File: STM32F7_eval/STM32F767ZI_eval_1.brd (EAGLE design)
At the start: 76.2 x 53.3 mm, 101 parts, among them CN3 GROVE-4P-CONN-I2C-90D, CN4 GROVE-4P-CONN-I2C-90D, CN5 ARDUINO_COMPAT_IF, CN6 STLINKV21_SWD_IF, CN7 WFT0750CZ09-SMD_, CN9 UART_IF, Q1 PMF370XN_, SW1 SKRPACE010_, SW2 SKRPACE010_, U1 STM32F767ZI_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

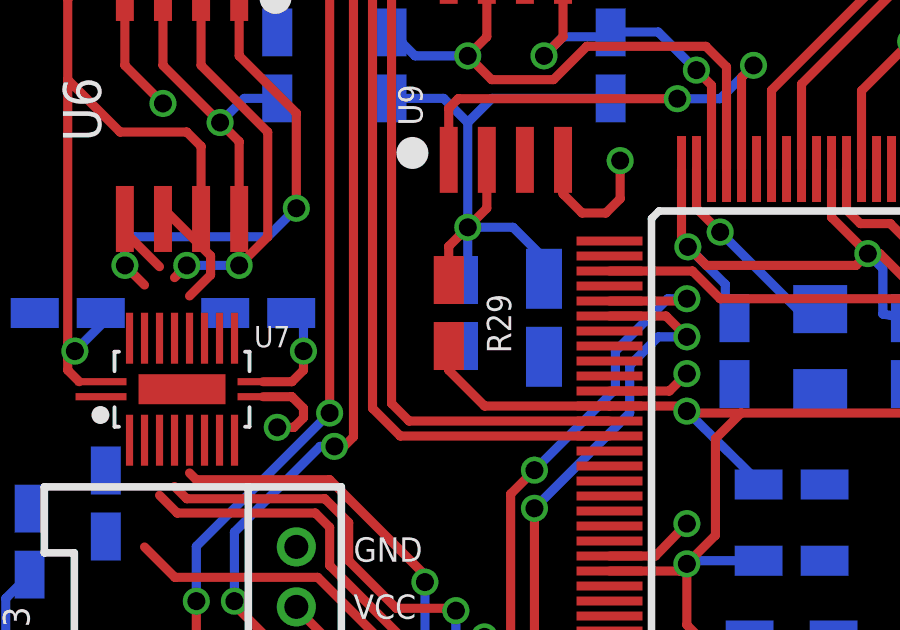
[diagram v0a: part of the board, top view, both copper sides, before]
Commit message: 回路図を修正
・回路図のレイアウトを修正
・定数変更
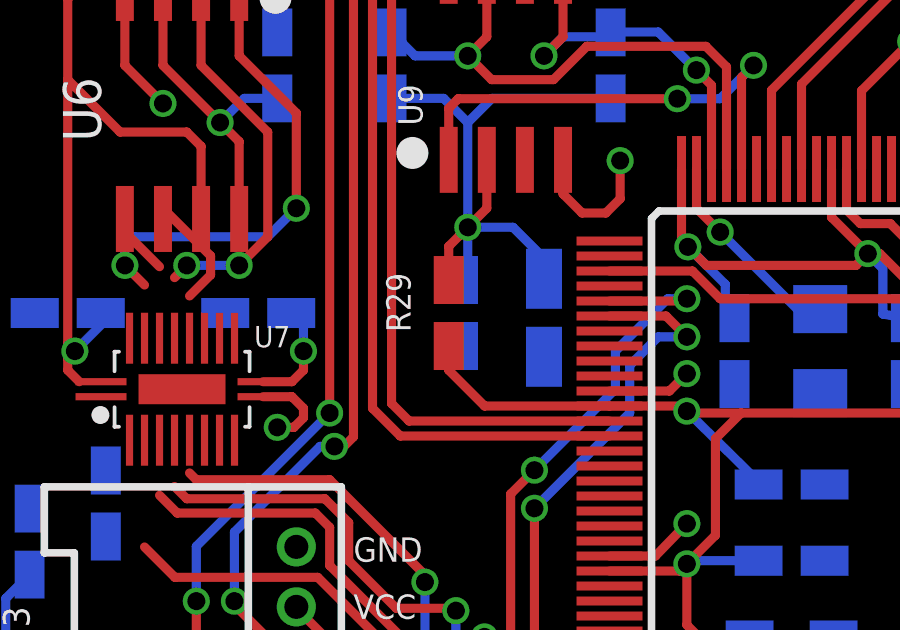
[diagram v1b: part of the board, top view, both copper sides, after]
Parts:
- R27, R28: value 3.3k -> 2.2k
- turned R29 to 90 degrees
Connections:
- net VCC_STSAFE: now also R29.2; no longer R29.1
- net VDD: now also R29.1; no longer R29.2
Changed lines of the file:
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@@
 <element name="C47" library="Parts" package="SMD_1608_DEV" value="0.1uF" x="15.71625" y="35.56" rot="MR270"/>
 <element name="C48" library="Parts" package="SMD_2012_DEV" value="10uF" x="18.415" y="35.40125" rot="MR270"/>
-<element name="R27" library="Parts" package="SMD_1608_DEV" value="3.3k" x="13.335" y="43.815" rot="MR270"/>
-<element name="R28" library="Parts" package="SMD_1608_DEV" value="3.3k" x="20.6375" y="43.815" rot="MR270"/>
+<element name="R27" library="Parts" package="SMD_1608_DEV" value="2.2k" x="13.335" y="43.815" rot="MR270"/>
+<element name="R28" library="Parts" package="SMD_1608_DEV" value="2.2k" x="20.6375" y="43.815" rot="MR270"/>
 <element name="U9" library="Parts" package="SO8N" value="STSAFE" x="17.145" y="43.815"/>
-<element name="R29" library="Parts" package="SMD_1608_DEV" value="0" x="15.24" y="35.56" rot="R270"/>
+<element name="R29" library="Parts" package="SMD_1608_DEV" value="0" x="15.24" y="35.56" rot="R90"/>
 <element name="U5" library="Parts" package="SC-70-5_DEV" value="MIC5366-1.8YC5_" x="-3.96875" y="-9.525"/>
 <element name="C28" library="Parts" package="SMD_1608_DEV" value="1uF X5R" x="-1.905" y="-24.4475"/>
@@
 <contactref element="U5" pad="2"/>
 <contactref element="C46" pad="2"/>
-<wire x1="71.585" y1="44.45" x2="71.585" y2="46.99" width="0" layer="19" extent="1-1"/>
-<wire x1="73.69" y1="35.2425" x2="73.37" y2="35.27" width="0" layer="19" extent="1-16"/>
-<wire x1="73.69" y1="39.0525" x2="74.295" y2="37.465" width="0" layer="19" extent="1-16"/>
-<wire x1="73.69" y1="32.385" x2="74.295" y2="34.6075" width="0" layer="19" extent="1-16"/>
-<wire x1="73.69" y1="24.4475" x2="73.69" y2="21.59" width="0" layer="19" extent="1-16"/>
-<wire x1="73.025" y1="6.6675" x2="73.46" y2="9.93" width="0" layer="19" extent="1-1"/>
-<wire x1="73.69" y1="27.94" x2="73.69" y2="24.4475" width="0" layer="19" extent="16-16"/>
-<wire x1="62.835" y1="28.8925" x2="68.74" y2="30.77" width="0" layer="19" extent="1-16"/>
-<wire x1="62.835" y1="33.02" x2="62.835" y2="28.8925" width="0" layer="19" extent="16-16"/>
-<wire x1="58.885" y1="33.27" x2="62.835" y2="33.02" width="0" layer="19" extent="16-16"/>
-<wire x1="58.885" y1="30.48" x2="58.885" y2="33.27" width="0" layer="19" extent="16-16"/>
-<wire x1="57.965" y1="29.845" x2="58.885" y2="30.48" width="0" layer="19" extent="1-16"/>
-<wire x1="58.885" y1="26.035" x2="57.965" y2="26.67" width="0" layer="19" extent="1-16"/>
-<wire x1="58.885" y1="21.9075" x2="57.965" y2="23.495" width="0" layer="19" extent="1-16"/>
-<wire x1="62.835" y1="24.13" x2="58.885" y2="26.035" width="0" layer="19" extent="16-16"/>
-<wire x1="63.5" y1="16.68" x2="57.615" y2="17.61" width="0" layer="19" extent="1-16"/>
-<wire x1="63.5" y1="7.825" x2="70.485" y2="9.93" width="0" layer="19" extent="1-16"/>
-<wire x1="63.61" y1="46.06" x2="68.06" y2="51.875" width="0" layer="19" extent="1-1"/>
-<wire x1="52.07" y1="8.89" x2="56.515" y2="16.51" width="0" layer="19" extent="1-1"/>
-<wire x1="49.53" y1="8.255" x2="52.07" y2="8.89" width="0" layer="19" extent="16-16"/>
-<wire x1="47.7725" y1="10.795" x2="49.53" y2="8.255" width="0" layer="19" extent="16-16"/>
-<wire x1="43.18" y1="2.54" x2="49.0075" y2="7.3025" width="0" layer="19" extent="16-16"/>
-<wire x1="40.64" y1="2.54" x2="43.18" y2="2.54" width="0" layer="19" extent="1-1"/>
-<wire x1="39.37" y1="8.89" x2="40.64" y2="2.54" width="0" layer="19" extent="1-1"/>
-<wire x1="37.57" y1="8.89" x2="39.37" y2="8.89" width="0" layer="19" extent="1-1"/>
-<wire x1="32.555" y1="9.525" x2="33.02" y2="11.58875" width="0" layer="19" extent="1-16"/>
-<wire x1="40.31125" y1="12.065" x2="38.27" y2="12.7" width="0" layer="19" extent="1-16"/>
-<wire x1="32.555" y1="6.985" x2="32.555" y2="9.525" width="0" layer="19" extent="16-16"/>
-<wire x1="25.37" y1="12.065" x2="29.39" y2="10.795" width="0" layer="19" extent="1-16"/>
-<wire x1="33.5" y1="18.06" x2="36.98875" y2="12.7" width="0" layer="19" extent="1-1"/>
-<wire x1="27.77" y1="21.8325" x2="28.5" y2="20.58" width="0" layer="19" extent="1-16"/>
-<wire x1="28.07" y1="24.4075" x2="27.77" y2="21.8325" width="0" layer="19" extent="16-16"/>
-<wire x1="27.77" y1="27.305" x2="28.07" y2="24.4075" width="0" layer="19" extent="16-16"/>
-<wire x1="27.77" y1="29.845" x2="27.77" y2="27.305" width="0" layer="19" extent="16-16"/>
-<wire x1="27.6225" y1="32.89" x2="27.77" y2="29.845" width="0" layer="19" extent="16-16"/>
-<wire x1="30.48" y1="33.19" x2="27.6225" y2="32.89" width="0" layer="19" extent="16-16"/>
-<wire x1="33.02" y1="33.19" x2="30.48" y2="33.19" width="0" layer="19" extent="16-16"/>
-<wire x1="35.73" y1="33.02" x2="33.02" y2="33.19" width="0" layer="19" extent="16-16"/>
-<wire x1="35.73" y1="35.56" x2="35.73" y2="33.02" width="0" layer="19" extent="16-16"/>
-<wire x1="34.21" y1="37.54" x2="35.73" y2="35.56" width="0" layer="19" extent="16-16"/>
-<wire x1="30.96" y1="37.54" x2="33.5" y2="38.25" width="0" layer="19" extent="1-1"/>
-<wire x1="24.765" y1="33.19" x2="27.6225" y2="32.89" width="0" layer="19" extent="16-16"/>
-<wire x1="23.1775" y1="33.54" x2="24.765" y2="33.19" width="0" layer="19" extent="16-16"/>
-<wire x1="18.415" y1="34.10125" x2="20.6" y2="32.96" width="0" layer="19" extent="1-16"/>
-<wire x1="15.71625" y1="34.46" x2="18.415" y2="34.10125" width="0" layer="19" extent="16-16"/>
-<wire x1="31.115" y1="25.23" x2="28.07" y2="24.4075" width="0" layer="19" extent="16-16"/>
-<wire x1="33.79" y1="25.23" x2="31.115" y2="25.23" width="0" layer="19" extent="16-16"/>
-<wire x1="36.83" y1="25.23" x2="33.79" y2="25.23" width="0" layer="19" extent="16-16"/>
-<wire x1="35.73" y1="29.845" x2="35.73" y2="33.02" width="0" layer="19" extent="16-16"/>
-<wire x1="39.37" y1="27.135" x2="36.83" y2="25.23" width="0" layer="19" extent="16-16"/>
-<wire x1="40.64" y1="27.94" x2="39.37" y2="27.135" width="0" layer="19" extent="16-16"/>
-<wire x1="23.495" y1="22.06625" x2="27.77" y2="21.8325" width="0" layer="19" extent="16-16"/>
-<wire x1="23.1775" y1="28.54" x2="22.5975" y2="32.96" width="0" layer="19" extent="1-1"/>
-<wire x1="19.685" y1="38.89375" x2="18.415" y2="34.10125" width="0" layer="19" extent="1-16"/>
-<wire x1="10.398125" y1="32.385" x2="15.71625" y2="34.46" width="0" layer="19" extent="1-16"/>
-<wire x1="7.79" y1="35.56" x2="9.05" y2="32.77" width="0" layer="19" extent="1-16"/>
-<wire x1="10.16" y1="27.765" x2="10.080625" y2="31.75" width="0" layer="19" extent="1-1"/>
-<wire x1="1.44" y1="35.56" x2="7.79" y2="35.56" width="0" layer="19" extent="16-16"/>
-<wire x1="3.81" y1="28.11" x2="10.16" y2="27.765" width="0" layer="19" extent="16-16"/>
-<wire x1="40" y1="40.36" x2="35.73" y2="35.56" width="0" layer="19" extent="1-16"/>
-<wire x1="47.16" y1="39.37" x2="41.25375" y2="42.4175" width="0" layer="19" extent="16-16"/>
-<wire x1="5.715" y1="42.545" x2="7.79" y2="35.56" width="0" layer="19" extent="16-16"/>
-<wire x1="9.525" y1="44.915" x2="5.715" y2="42.545" width="0" layer="19" extent="16-16"/>
-<wire x1="26.416" y1="50.8" x2="28.5" y2="40.36" width="0" layer="19" extent="1-1"/>
-<wire x1="10.16" y1="16.335" x2="20.6" y2="20.96" width="0" layer="19" extent="1-1"/>
-<wire x1="7.62" y1="2.54" x2="10.16" y2="16.335" width="0" layer="19" extent="1-1"/>
-<wire x1="-3.96875" y1="-10.95" x2="7.62" y2="2.54" width="0" layer="19" extent="1-1"/>
-<wire x1="-0.205" y1="-17.4625" x2="-3.96875" y2="-10.95" width="0" layer="19" extent="1-1"/>
-<wire x1="-0.805" y1="-24.4475" x2="-0.205" y2="-17.4625" width="0" layer="19" extent="1-1"/>
-<wire x1="-0.805" y1="-29.36875" x2="-0.805" y2="-24.4475" width="0" layer="19" extent="1-1"/>
+<wire x1="-0.805" y1="-24.4475" x2="-0.805" y2="-29.36875" width="0" layer="19" extent="1-1"/>
+<wire x1="-0.205" y1="-17.4625" x2="-0.805" y2="-24.4475" width="0" layer="19" extent="1-1"/>
+<wire x1="-3.96875" y1="-10.95" x2="-0.205" y2="-17.4625" width="0" layer="19" extent="1-1"/>
+<wire x1="7.62" y1="2.54" x2="-3.96875" y2="-10.95" width="0" layer="19" extent="1-1"/>
 </signal>
 <signal name="N$2">
@@
 <wire x1="29" y1="19.33" x2="30.71" y2="21.04" width="0.3048" layer="1"/>
 <wire x1="16.435" y1="32.46" x2="15.24" y2="33.655" width="0.3048" layer="1"/>
-<wire x1="15.24" y1="33.655" x2="15.24" y2="34.46" width="0.3048" layer="1"/>
 <wire x1="38.735" y1="32.22625" x2="24.98625" y2="32.22625" width="0.3048" layer="1"/>
 <wire x1="38.735" y1="32.22625" x2="39.608125" y2="31.353125" width="0.3048" layer="1"/>
@@
 <wire x1="23.555625" y1="20.46" x2="23.733125" y2="20.6375" width="0.3048" layer="1"/>
 <contactref element="CN4" pad="3"/>
-<contactref element="R29" pad="2"/>
 <wire x1="13.49375" y1="12.3825" x2="11.54125" y2="14.335" width="0.3048" layer="1"/>
 <wire x1="10.16" y1="14.335" x2="11.54125" y2="14.335" width="0.3048" layer="1"/>
+<contactref element="R29" pad="1"/>
+<wire x1="15.24" y1="34.46" x2="15.24" y2="33.655" width="0.3048" layer="1"/>
 </signal>
 <signal name="PD9">
@@
 <wire x1="20.6375" y1="42.715" x2="16.68" y2="42.715" width="0.3048" layer="16"/>
 <wire x1="16.68" y1="42.715" x2="15.875" y2="41.91" width="0.3048" layer="16"/>
-<wire x1="15.24" y1="36.66" x2="15.24" y2="37.068125" width="0.3048" layer="1"/>
-<wire x1="15.24" y1="36.66" x2="15.24" y2="37.7825" width="0.3048" layer="1"/>
 <wire x1="15.24" y1="37.7825" x2="15.875" y2="38.4175" width="0.3048" layer="1"/>
 <wire x1="15.875" y1="38.4175" x2="16.51" y2="39.0525" width="0.3048" layer="1"/>
 <contactref element="R27" pad="2"/>
 <contactref element="R28" pad="2"/>
-<contactref element="R29" pad="1"/>
 <contactref element="U9" pad="2"/>
 <contactref element="C48" pad="1"/>
@@
 <wire x1="16.51" y1="40.665" x2="16.51" y2="39.0525" width="0.3048" layer="1"/>
 <wire x1="13.335" y1="42.715" x2="15.07" y2="42.715" width="0.3048" layer="16"/>
+<contactref element="R29" pad="2"/>
+<wire x1="15.24" y1="36.66" x2="15.24" y2="37.7825" width="0.3048" layer="1"/>
 </signal>
 <signal name="+1V8">

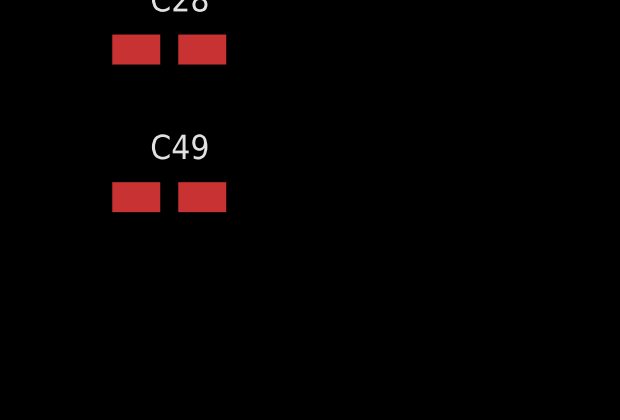
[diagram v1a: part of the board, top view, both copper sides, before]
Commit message: 回路図を修正
・回路図のレイアウトを修正
・ダンピング抵抗追加
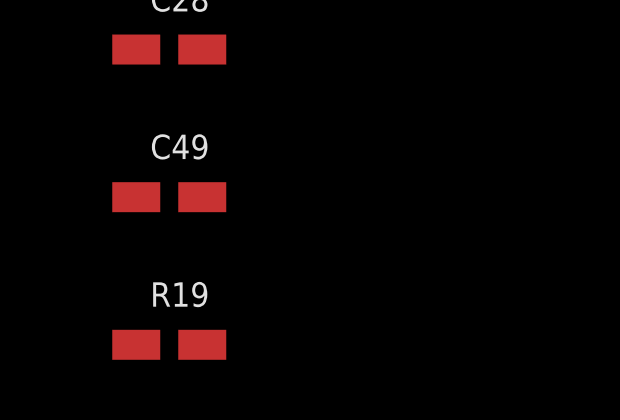
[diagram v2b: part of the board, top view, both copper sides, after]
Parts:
- added R19: 10, Parts:SMD_1608_DEV
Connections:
- new net PC10_D: R19.1, U7.16
- net PC10: now also R19.2; no longer U7.16
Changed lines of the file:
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@@
 <element name="C29" library="Parts" package="C1210_TPST_DEV" value="10uF" x="-1.905" y="-17.4625"/>
 <element name="C49" library="Parts" package="SMD_1608_DEV" value="1uF X5R" x="-1.905" y="-29.36875"/>
+<element name="R19" library="Parts" package="SMD_1608_DEV" value="10" x="-1.905" y="-34.29"/>
 </elements>
 <signals>
@@
 <wire x1="11.27125" y1="30.00375" x2="14.44625" y2="26.82875" width="0.3048" layer="1"/>
 <wire x1="14.44625" y1="26.590625" x2="14.44625" y2="26.82875" width="0.3048" layer="1"/>
-<contactref element="U7" pad="16"/>
-<wire x1="6.6" y1="30.23" x2="6.1" y2="34.72" width="0" layer="19" extent="1-1"/>
+<contactref element="R19" pad="2"/>
+<wire x1="-0.805" y1="-34.29" x2="23.97125" y2="15.08125" width="0" layer="19" extent="1-1"/>
 </signal>
 <signal name="PC11">
@@
 <wire x1="15.24" y1="40.665" x2="15.24" y2="42.38625" width="0.3048" layer="1"/>
 </signal>
+<signal name="PC10_D">
+<contactref element="R19" pad="1"/>
+<contactref element="U7" pad="16"/>
+<wire x1="-3.005" y1="-34.29" x2="6.1" y2="34.72" width="0" layer="19" extent="1-1"/>
+</signal>
 </signals>

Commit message: 回路図を修正
・ST-LINK V2-1インターフェースを他部品に変更
・外部フラッシュの電源をSTMの電源と切り離す
・Groveコネクターを基板の隅に移動
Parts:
- removed CN4: GROVE-4P-CONN-I2C-90D, PartsForProto:GROVE-4P-90D
- removed CN6: STLINKV21_SWD_IF, PartsForProto:STLINKV21_SWD_H6
- added CN1: STLINKV2_SWD_IF_, Connectors:DF65-7P-1.7V_DEV
- added CN2: GROVE-4P-CONN-I2C-90D, PartsForProto:GROVE-4P-90D
- moved R19 59.3 mm to (12.7, 23.2)
- moved C28 46.9 mm to (10.5, 20.8), flipped to the bottom, turned to 90 degrees
- moved C49 45.6 mm to (10.3, 14.6), flipped to the bottom, turned to 270 degrees
- moved C29 37.0 mm to (3.81, 19.1), flipped to the bottom
- moved U5 31.9 mm to (12.5, 17.8)
- moved C42 30.9 mm to (6.83, 13.0)
- moved U6 24.8 mm to (5.71, 17.8)
- moved R25 21.4 mm to (5.40, 6.99)
- moved CN3 12.1 mm to (8.89, 36.8)
- moved R5 4.84 mm to (10.8, 31.1), turned to 0 degrees
- moved C45 4.63 mm to (1.43, 25.2)
- moved U7 4.49 mm to (5.71, 28.6)
- moved C46 3.02 mm to (2.38, 32.5), turned to 90 degrees
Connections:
- new net EXT_3V3: CN2.3, CN3.3, R25.1
- net +3V3: no longer R25.1
- net 0V: now also CN1.2, CN2.4; no longer CN4.4, CN6.3
- net NRST: now also CN1.4; no longer CN6.5
- net PB8: now also CN2.1; no longer CN4.1
- net PB9: now also CN2.2; no longer CN4.2
- net PD8: now also CN1.6; no longer CN6.7
- net PD9: now also CN1.7; no longer CN6.8
- net SWO: now also CN1.5; no longer CN6.6
- net TCK: now also CN1.1; no longer CN6.2
- net TMS: now also CN1.3; no longer CN6.4
- net VDD: no longer CN3.3, CN4.3
- net VIN: no longer CN6.9
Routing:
- net +3V3: track 113.3 -> 53.3 mm, vias 4 -> 3
- net VDD: track 282.0 -> 237.2 mm, vias 23 -> 21
- net +1V8: track 40.9 -> 0.00 mm, vias 2 -> 0
- net PH0: track 29.7 -> 4.80 mm, vias 2 -> 1
- net !CS!: track 15.9 -> 0.00 mm, vias 2 -> 0
- net EXT_3V3: track 0.00 -> 15.5 mm
- net PA15: track 25.2 -> 10.4 mm
- net PC12: track 31.1 -> 16.6 mm
- net PC11: track 29.8 -> 16.9 mm
- net SO: track 12.9 -> 0.00 mm, vias 2 -> 0
- net PC10: track 27.9 -> 16.5 mm
- net VIN: track 58.6 -> 50.5 mm
- net PD9: track 40.4 -> 33.6 mm
- net NRST: track 117.2 -> 110.8 mm
- net PD8: track 40.9 -> 35.2 mm
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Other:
- board text removed: "A0"
- board text removed: "A1"
- board text removed: "GND"
- board text removed: "SCL"
- board text removed: "SDA"
- board text removed: "VCC"

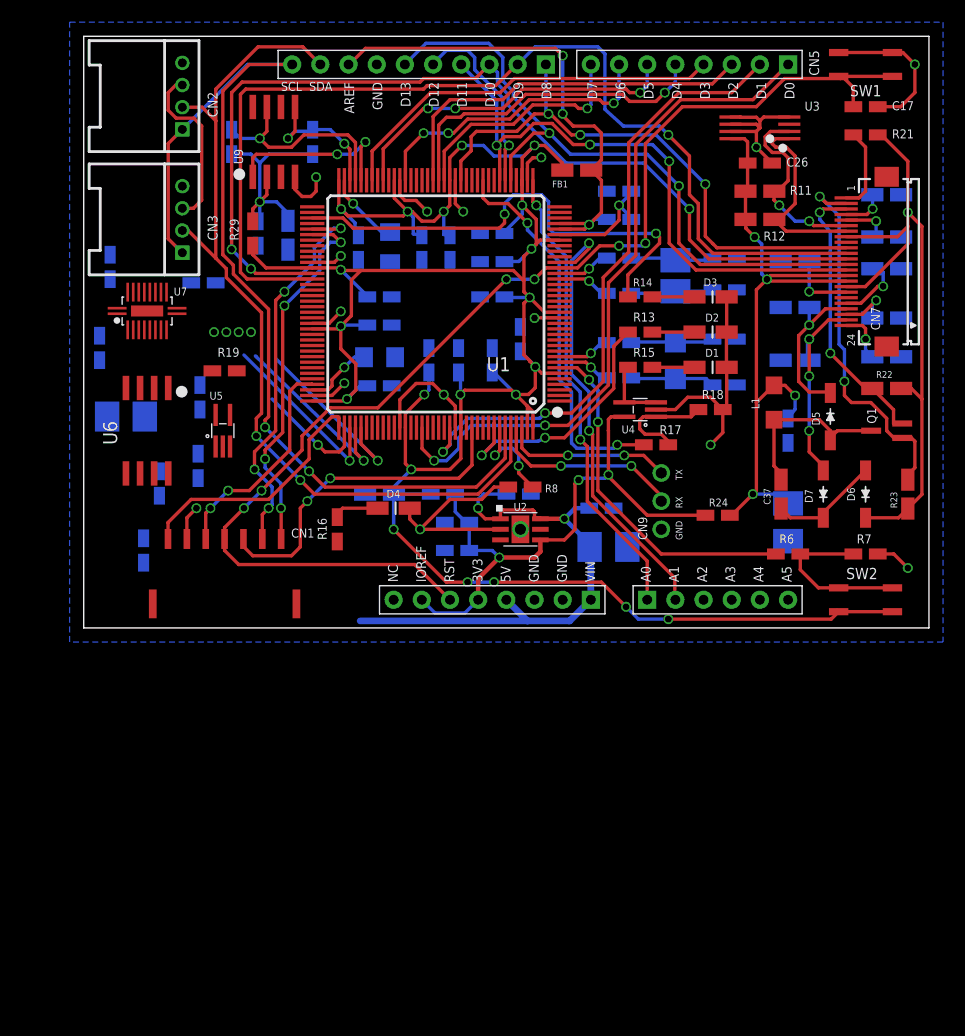
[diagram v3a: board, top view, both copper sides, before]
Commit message: 回路図を修正
・配線変更
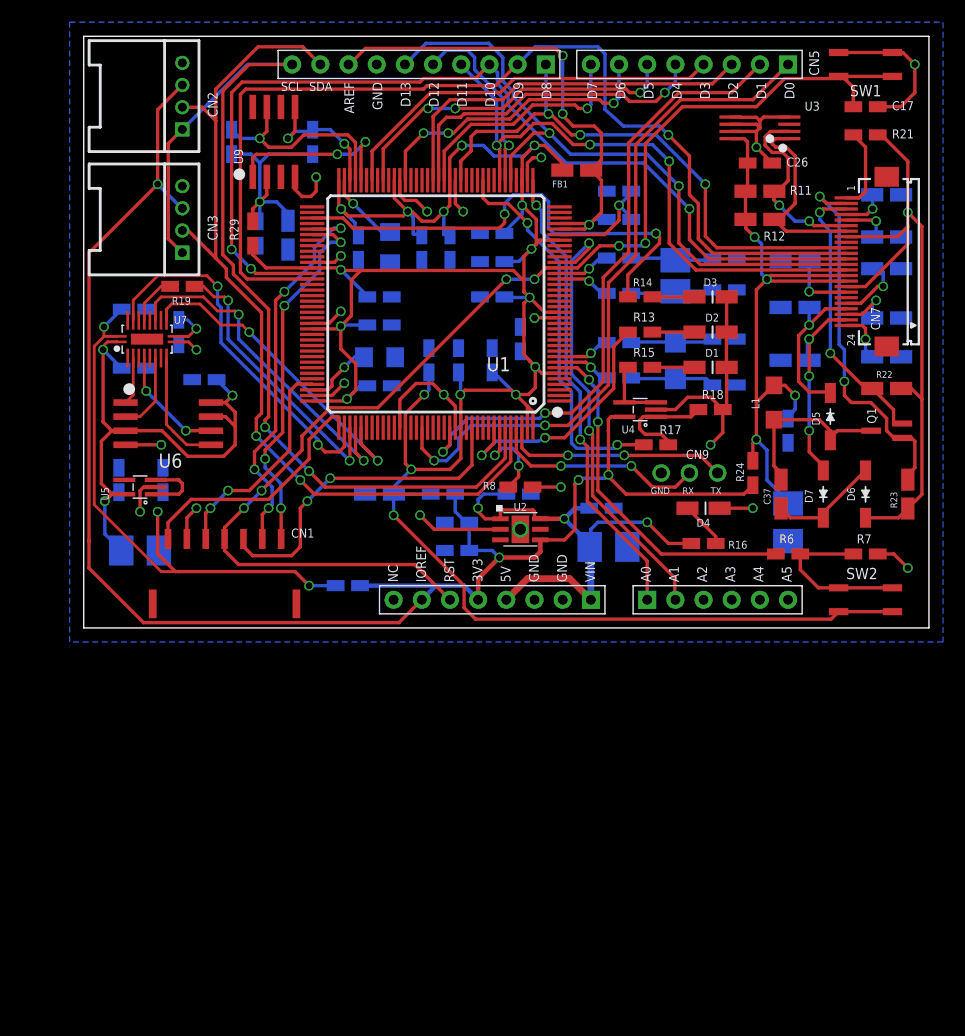
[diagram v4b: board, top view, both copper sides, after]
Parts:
- moved R16 33.0 mm to (55.9, 7.62), turned to 180 degrees
- moved D4 27.9 mm to (55.9, 10.8)
- moved R25 18.7 mm to (23.8, 3.81), turned to 0 degrees
- moved C29 12.1 mm to (5.08, 6.99), turned to 180 degrees
- moved U5 9.03 mm to (5.08, 12.7), turned to 90 degrees
- moved R19 8.52 mm to (8.89, 30.8)
- moved CN9 5.08 mm to (52.1, 14.0), turned to 0 degrees
- moved R5 4.97 mm to (8.57, 26.7), turned to 90 degrees
- moved R24 4.96 mm to (60.3, 14.0), turned to 90 degrees
- moved C46 4.37 mm to (4.52, 28.7), turned to 180 degrees
- moved C42 3.67 mm to (3.17, 13.3)
- moved C45 3.59 mm to (4.52, 23.4), turned to 180 degrees
- moved C49 3.42 mm to (7.14, 13.3), turned to 90 degrees
- moved U7 2.54 mm to (5.71, 26.0)
- moved U6 2.01 mm to (7.62, 18.4), turned to 270 degrees
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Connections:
- removed net EXT_3V3: CN2.3, CN3.3, R25.1
- net +3V3: now also CN2.3, CN3.3, R25.1
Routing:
- net +3V3: track 53.3 -> 147.0 mm, vias 3 -> 4
- net VCC_MEM: track 0.00 -> 56.7 mm, vias 0 -> 3
- net +1V8: track 0.00 -> 50.7 mm, vias 0 -> 3
- net PA15: track 10.4 -> 33.3 mm
- net EXT_3V3: track 15.5 -> 0.00 mm
- net PC11: track 16.9 -> 31.2 mm
- net PC12: track 16.6 -> 29.7 mm
- net SI: track 0.00 -> 10.8 mm
- net SCLK: track 0.00 -> 10.4 mm, vias 0 -> 2
- net PC10: track 16.5 -> 25.5 mm
- net SO: track 0.00 -> 7.17 mm
- net PE1: track 15.3 -> 20.4 mm
- net PC10_D: track 0.00 -> 4.50 mm
- net !CS!: track 0.00 -> 4.30 mm
- net !OE!: track 0.00 -> 3.95 mm, vias 0 -> 1
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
